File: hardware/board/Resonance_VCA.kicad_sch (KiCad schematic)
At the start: 32 parts

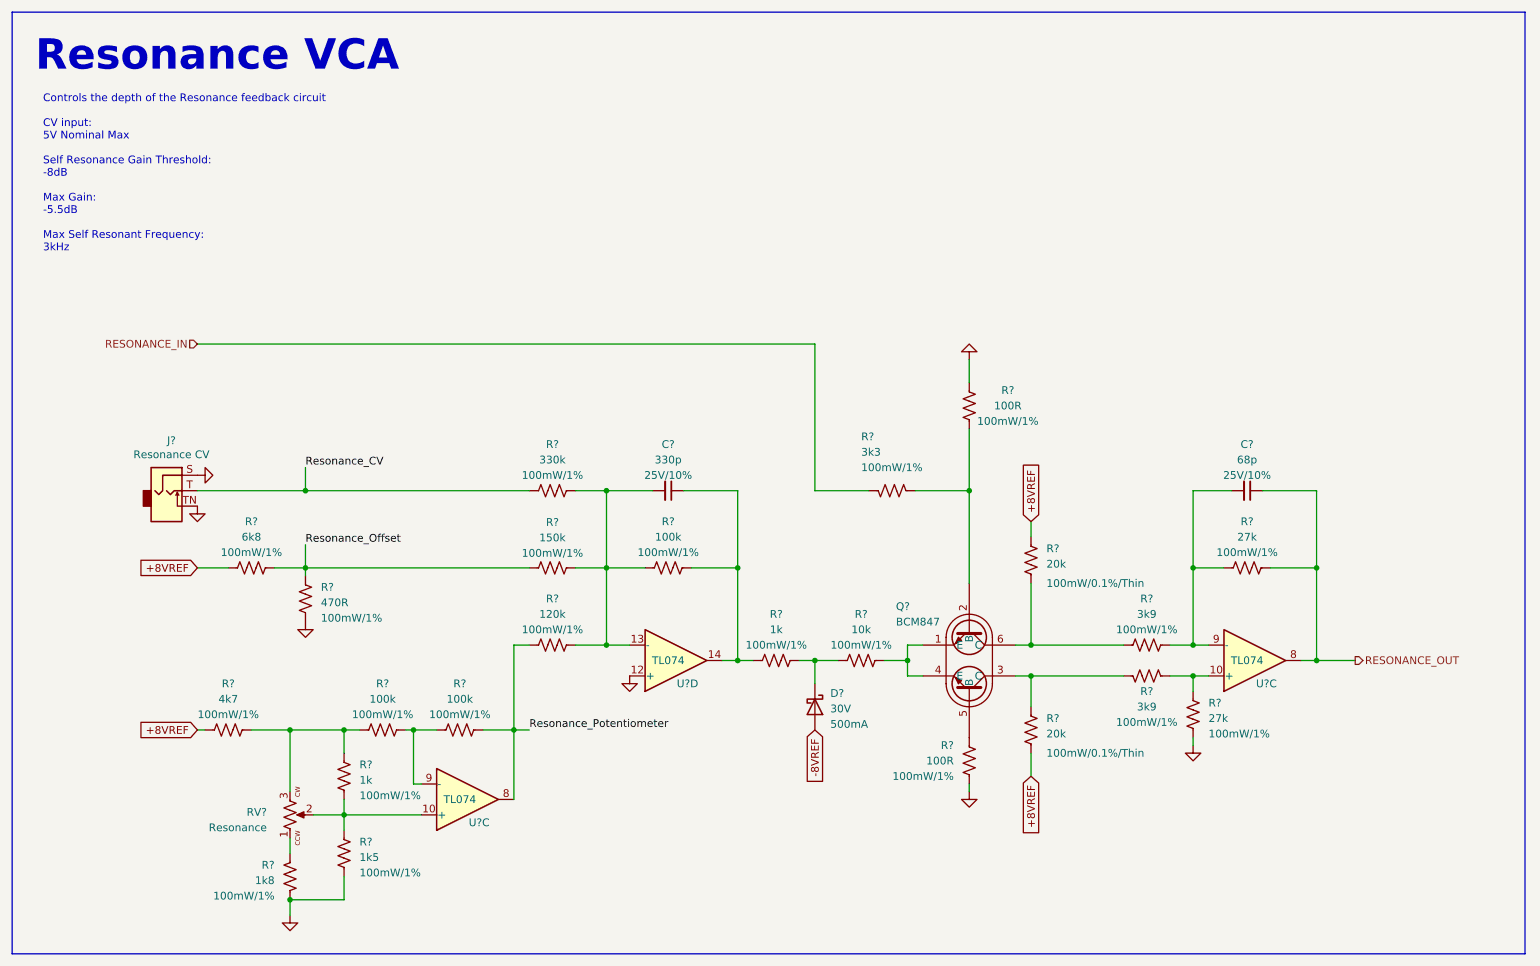
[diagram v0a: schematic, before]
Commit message: Schematic getting closer to being finished
Schematic should be close to being ready to assign MPNs.
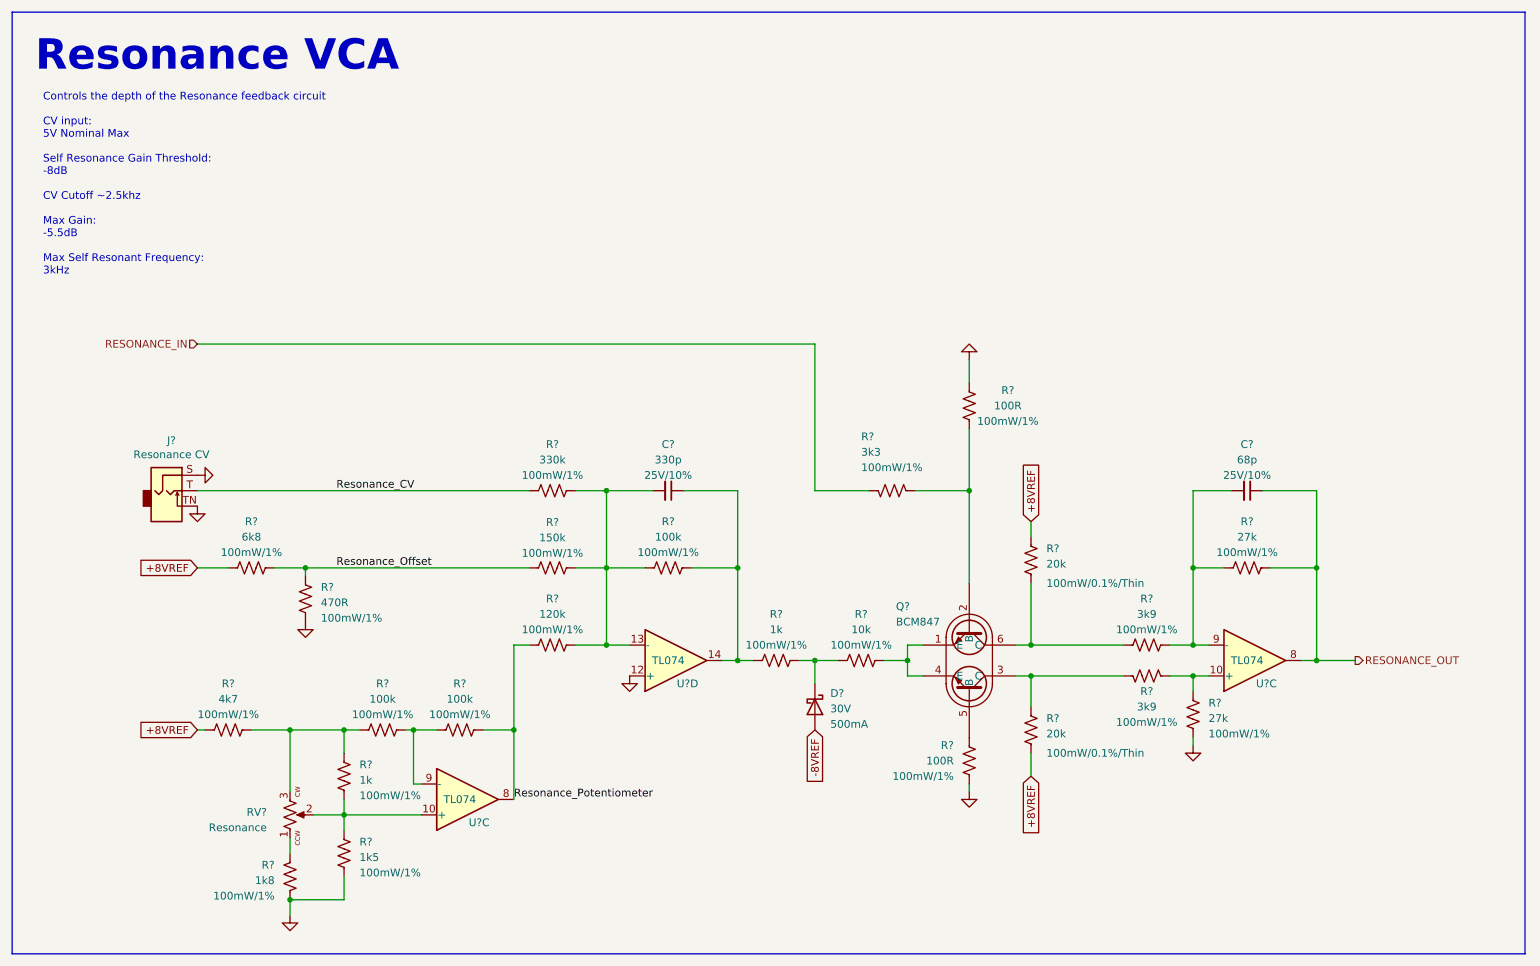
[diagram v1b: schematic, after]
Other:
- note added: "Controls the depth of the Resonance feedback circuit CV input: 5V Nominal Max Self Resonance Gain Threshold: -8dB CV Cutoff ~2.5khz Max Gain: -5.5dB Max Self Resonant Frequency: 3kHz"
- note removed: "Controls the depth of the Resonance feedback circuit CV input: 5V Nominal Max Self Resonance Gain Threshold: -8dB Max Gain: -5.5dB Max Self Resonant Frequency: 3kHz"
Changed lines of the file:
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@@
   (junction (at 172.72 93.98) (diameter 0) (color 0 0 0 0)
   )
-  (junction (at 63.5 93.98) (diameter 0) (color 0 0 0 0)
-  )
   (junction (at 134.62 121.92) (diameter 0) (color 0 0 0 0)
   )
@@
     (stroke (width 0) (type default))
   )
-  (wire (pts (xy 97.79 133.35) (xy 100.33 133.35))
-    (stroke (width 0) (type default))
-  )
   (wire (pts (xy 182.88 99.06) (xy 182.88 101.6))
     (stroke (width 0) (type default))
@@
     (stroke (width 0) (type default))
   )
-  (wire (pts (xy 45.72 93.98) (xy 63.5 93.98))
+  (wire (pts (xy 45.72 93.98) (xy 100.33 93.98))
     (stroke (width 0) (type default))
   )
@@
     (stroke (width 0) (type default))
   )
-  (wire (pts (xy 63.5 90.17) (xy 63.5 93.98))
-    (stroke (width 0) (type default))
-  )
   (wire (pts (xy 172.72 93.98) (xy 172.72 109.22))
     (stroke (width 0) (type default))
@@
     (stroke (width 0) (type default))
   )
-  (wire (pts (xy 63.5 102.87) (xy 63.5 106.68))
-    (stroke (width 0) (type default))
-  )
   (wire (pts (xy 229.87 121.92) (xy 236.22 121.92))
     (stroke (width 0) (type default))
@@
   )
   (wire (pts (xy 60.96 133.35) (xy 60.96 143.51))
-    (stroke (width 0) (type default))
-  )
-  (wire (pts (xy 63.5 93.98) (xy 100.33 93.98))
     (stroke (width 0) (type default))
   )
@@
     (effects (font (size 5 5) (thickness 0.508) bold) (justify left bottom))
   )
-  (text "Controls the depth of the Resonance feedback circuit \n\nCV input:\n5V Nominal Max\n\nSelf Resonance Gain Threshold:\n-8dB\n\nMax Gain:\n-5.5dB\n\nMax Self Resonant Frequency:\n3kHz\n\n\n\n"
-    (at 20.32 60.96 0)
-    (effects (font (size 1.27 1.27)) (justify left bottom))
-  )
-  (label "Resonance_Offset" (at 63.5 102.87 0) (fields_autoplaced)
-    (effects (font (size 1.27 1.27)) (justify left bottom))
-  )
-  (label "Resonance_CV" (at 63.5 90.17 0) (fields_autoplaced)
-    (effects (font (size 1.27 1.27)) (justify left bottom))
-  )
-  (label "Resonance_Potentiometer" (at 100.33 133.35 0) (fields_autoplaced)
-    (effects (font (size 1.27 1.27)) (justify left bottom))
-  )
+  (text "Controls the depth of the Resonance feedback circuit \n\nCV input:\n5V Nominal Max\n\nSelf Resonance Gain Threshold:\n-8dB\n\nCV Cutoff ~2.5khz\n\nMax Gain:\n-5.5dB\n\nMax Self Resonant Frequency:\n3kHz\n\n\n\n"
+    (at 20.32 64.77 0)
+    (effects (font (size 1.27 1.27)) (justify left bottom))
+  )
+  (label "Resonance_Offset" (at 68.58 106.68 0) (fields_autoplaced)
+    (effects (font (size 1.27 1.27)) (justify left bottom))
+  )
+  (label "Resonance_CV" (at 68.58 93.98 0) (fields_autoplaced)
+    (effects (font (size 1.27 1.27)) (justify left bottom))
+  )
+  (label "Resonance_Potentiometer" (at 97.79 144.78 0) (fields_autoplaced)
+    (effects (font (size 1.27 1.27)) (justify left bottom))
+  )

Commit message: BOM Consolidation
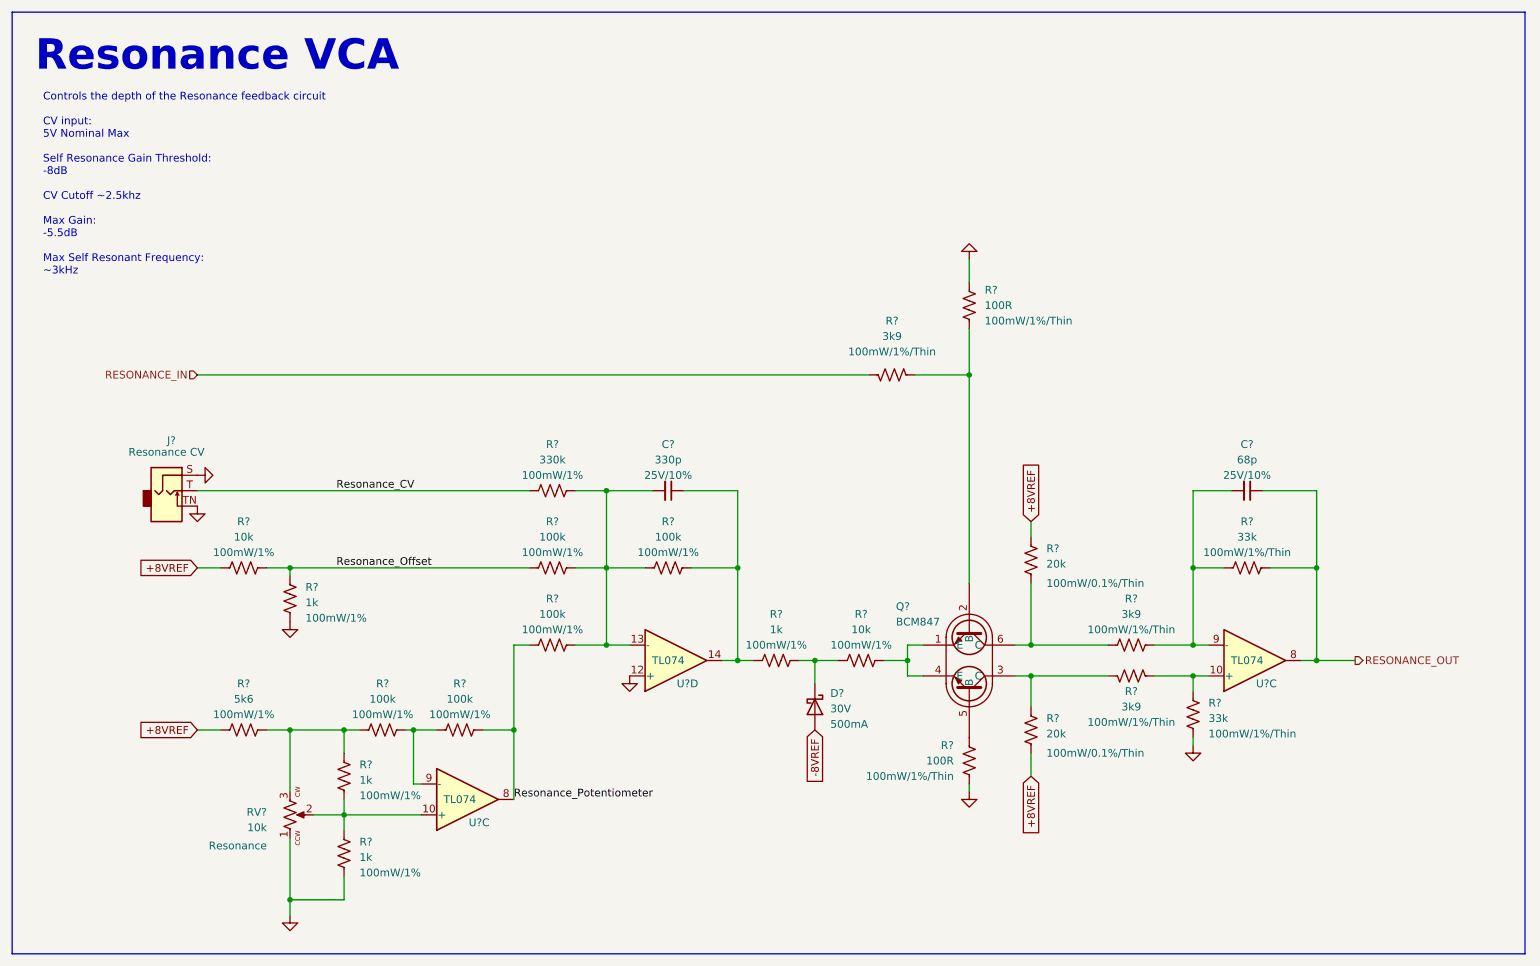
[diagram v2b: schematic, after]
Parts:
- removed R?: 330k, winterbloom:R_0603_HandSolder, symbol Device:R_US
- removed R?: 1k8, winterbloom:R_0603_HandSolder, symbol Device:R_US
- added R?: 330k, winterbloom:R_0603_HandSolder, symbol Device:R_US
- J?: value Resonance CV -> ~; Name (none) -> Resonance CV
- R? (x2): value 27k -> 33k; Rating 100mW/1% -> 100mW/1%/Thin
- R? (x4): Rating 100mW/1% -> 100mW/1%/Thin
- R?: value 150k -> 100k
- R?: value 1k5 -> 1k
- R?: value 3k3 -> 3k9; Rating 100mW/1% -> 100mW/1%/Thin
- R?: value 470R -> 1k
- R?: value 120k -> 100k
- R?: value 6k8 -> 10k
- R?: value 4k7 -> 5k6
- RV?: value Resonance -> 10k; Name (none) -> Resonance
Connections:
- net GND: now also RV?.1
- net Resonance_CV: now also R?.2
- net at C?.2, R?.1, R?.1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: now also R?.1
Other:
- note added: "Controls the depth of the Resonance feedback circuit CV input: 5V Nominal Max Self Resonance Gain Threshold: -8dB CV Cutoff ~2.5khz Max Gain: -5.5dB Max Self Resonant Frequency: ~3kHz"
- note removed: "Controls the depth of the Resonance feedback circuit CV input: 5V Nominal Max Self Resonance Gain Threshold: -8dB CV Cutoff ~2.5khz Max Gain: -5.5dB Max Self Resonant Frequency: 3kHz"
- moved on the sheet: R?

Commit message: Updates for LED Drivers
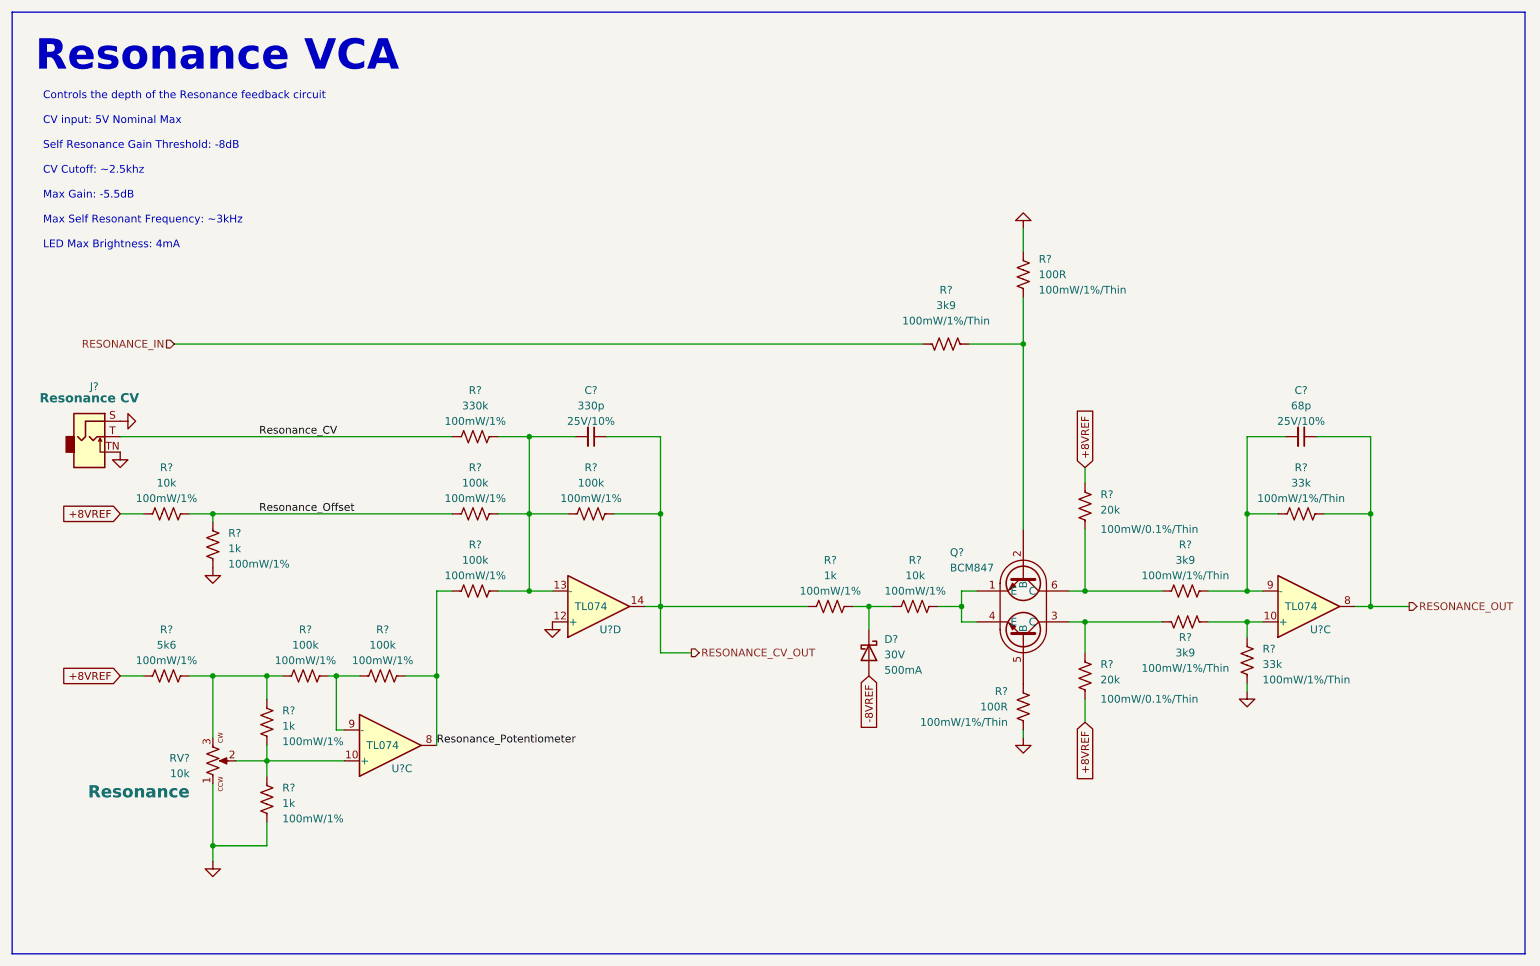
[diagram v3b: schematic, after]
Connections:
- net RESONANCE_CV_OUT: now reaches C?.1, R?.1, R?.2, U?.14
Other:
- note added: "Controls the depth of the Resonance feedback circuit CV input: 5V Nominal Max Self Resonance Gain Threshold: -8dB CV Cutoff: ~2.5khz Max Gain: -5.5dB Max Self Resonant Frequency: ~3kHz LED Max Brightness: 4mA"
- note removed: "Controls the depth of the Resonance feedback circuit CV input: 5V Nominal Max Self Resonance Gain Threshold: -8dB CV Cutoff ~2.5khz Max Gain: -5.5dB Max Self Resonant Frequency: ~3kHz"
- moved on the sheet: C?, D?, J?, Q?, R?, RV?, U?C, U?D

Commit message: hardware: update schematic with footprints and preliminary MPNs
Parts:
- C? (x2): Notes 0603, 25V+, 10% -> (none); smd kit 1 -> (none)
- D?: value 30V -> BAS315; footprint winterbloom:D_SOD-123+SOD-123F -> winterbloom:D_SOD-323; MPN (none) -> BAS316,115; Notes Any PMEGxxxxEGW part, 500mA If -> Clipping diode; Rating 500mA -> 1Vf @ 100mA; mpn PMEG2005EGWX -> (none); smd kit 1 -> (none)
- J?: mpn WQP-WQP518MA -> (none)
- Q?: LCSC C396099 -> (none); LCSC Extended YES -> (none); Manufacturer Nexperia -> (none)
- R? (x22): smd kit 1 -> (none)
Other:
- title: Diode Ladder Filter -> Neptune

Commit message: Very first component layout.
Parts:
- removed U?: TL074, Package_SO:TSSOP-14_4.4x5mm_P0.65mm, symbol winterbloom:TL074
- added U?: TL074, Package_SO:TSSOP-14_4.4x5mm_P0.65mm, symbol winterbloom:TL074
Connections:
- net RESONANCE_OUT: now also U?.8
- net Resonance_Potentiometer: now also U?.14; no longer U?.8
- net at R?.1, R?.1: now also U?.10 (+)
- net at R?.1, R?.2: now also U?.13 (-); no longer U?.9 (-)
- net at R?.1, R?.2, RV?.2: now also U?.12 (+); no longer U?.10 (+)
- net at C?.2, R?.1, R?.2: now also U?.9 (-)
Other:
- moved on the sheet: U?C

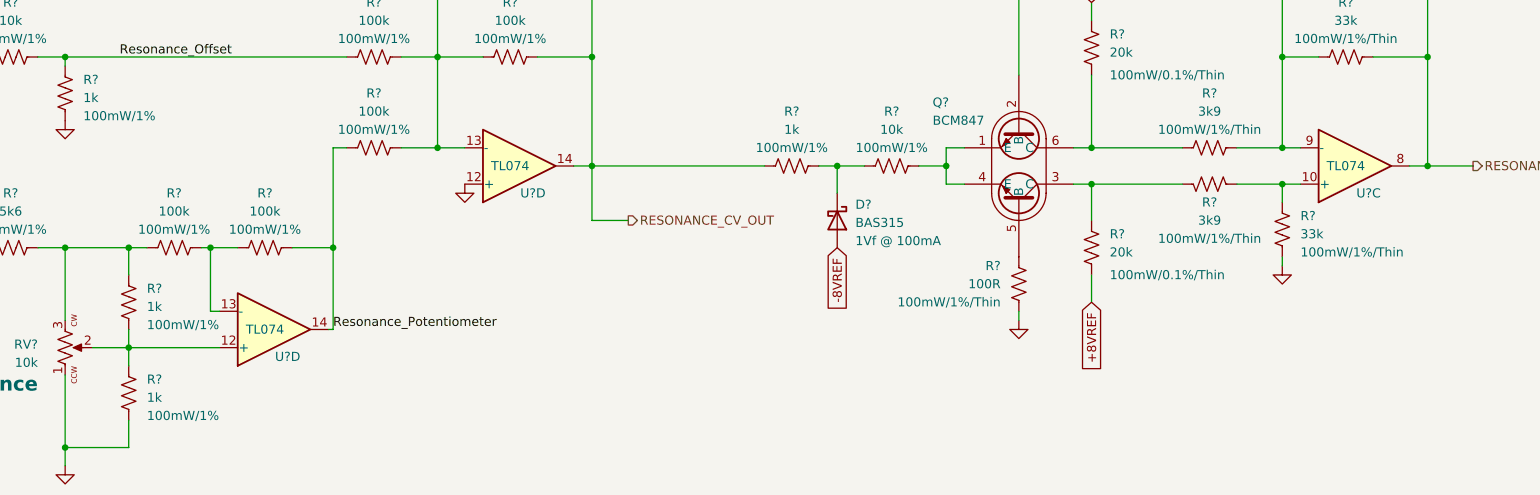
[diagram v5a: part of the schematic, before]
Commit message: First Draft of layout V2 (All components facing the same way)
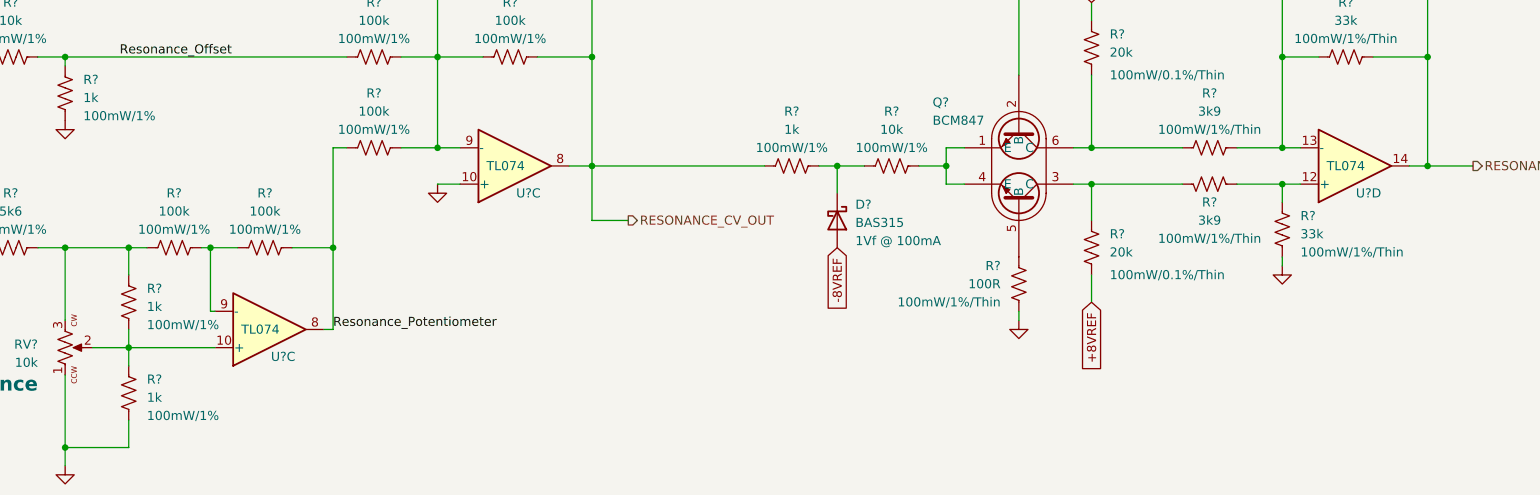
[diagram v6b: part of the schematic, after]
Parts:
- removed U?: TL074, Package_SO:TSSOP-14_4.4x5mm_P0.65mm, symbol winterbloom:TL074
- added U?: TL074, Package_SO:TSSOP-14_4.4x5mm_P0.65mm, symbol winterbloom:TL074
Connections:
- net GND: now also U?.10 (+); no longer U?.12 (+)
- net RESONANCE_CV_OUT: now also U?.8; no longer U?.14
- net RESONANCE_OUT: now also U?.14; no longer U?.8
- net Resonance_Potentiometer: now also U?.8
- net at R?.1, R?.1: now also U?.12 (+); no longer U?.10 (+)
- net at R?.1, R?.2: now also U?.9 (-)
- net at R?.1, R?.2, RV?.2: now also U?.10 (+)
- net at C?.2, R?.1, R?.2: now also U?.13 (-); no longer U?.9 (-)
- net at C?.2, R?.1, R?.1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: now also U?.9 (-); no longer U?.13 (-)
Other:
- moved on the sheet: U?C, U?D
